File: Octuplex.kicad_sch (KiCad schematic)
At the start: 9 parts, among them U1 MC68B09, U2 MC68B40, U3 MC68B50, U4 27128, U5 HM62256BLP, U6 74LS139, X1 CXO_DIP8, X2 CXO_DIP8

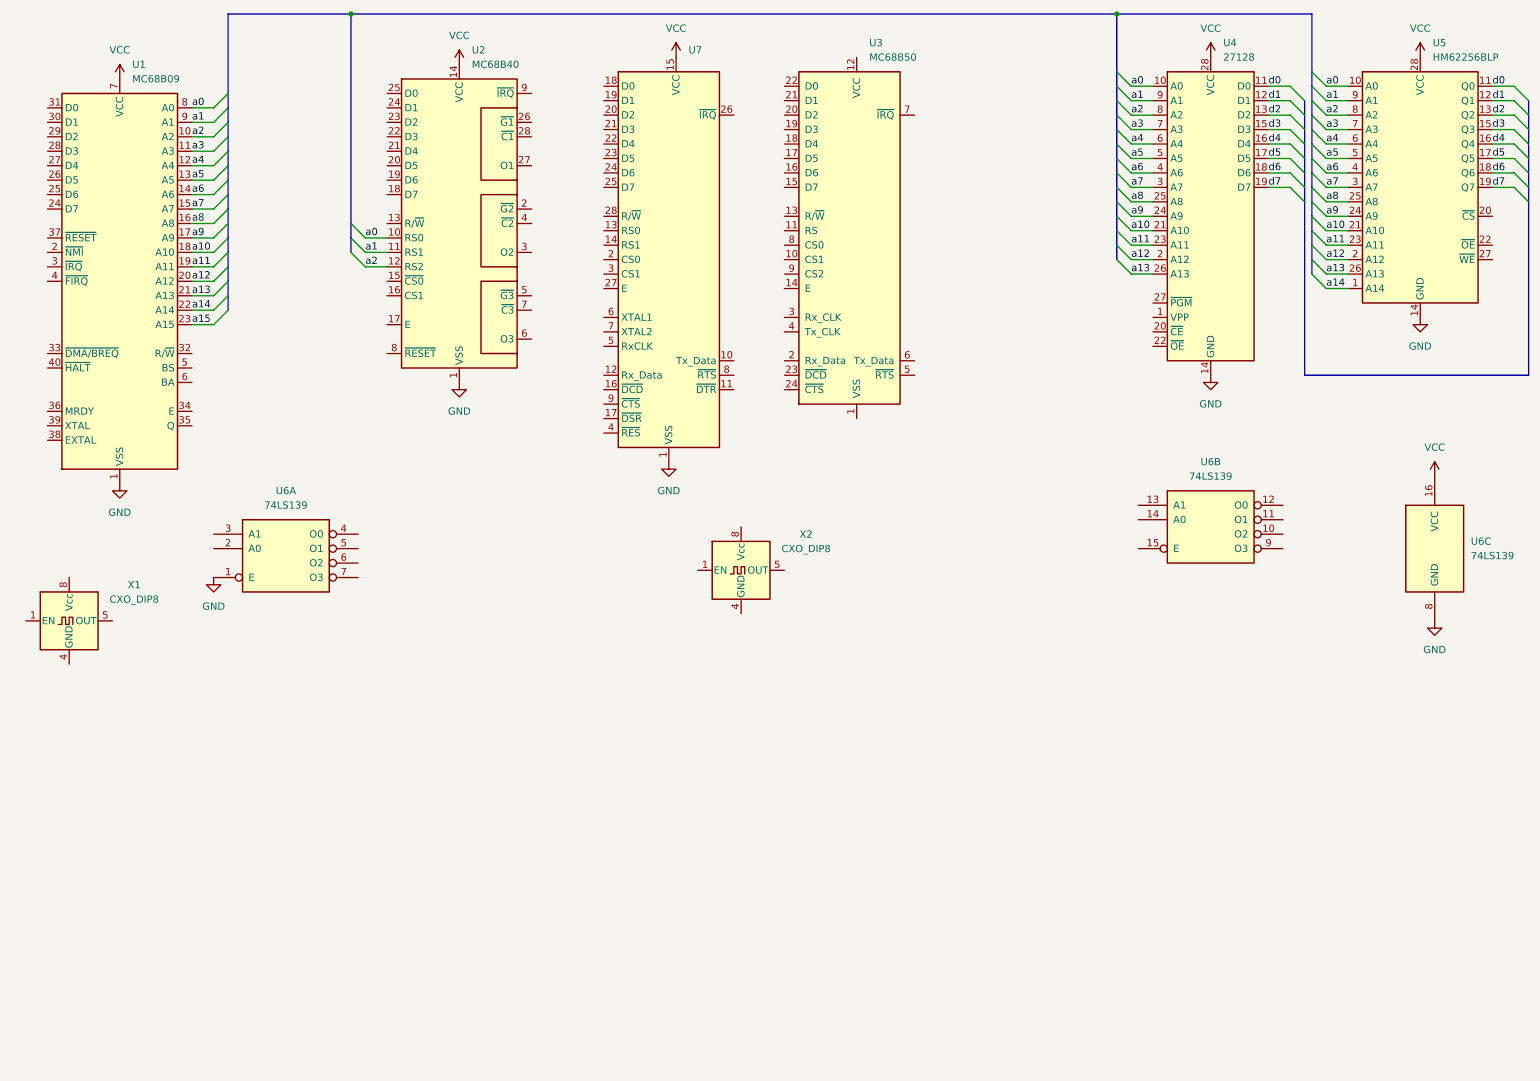
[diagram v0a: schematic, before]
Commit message: WIP: new symbols, initial PCB.
Add 6502 and 6522 symbols. Add mounting holes, board edge, and parts to PCB. Begin wiring up.
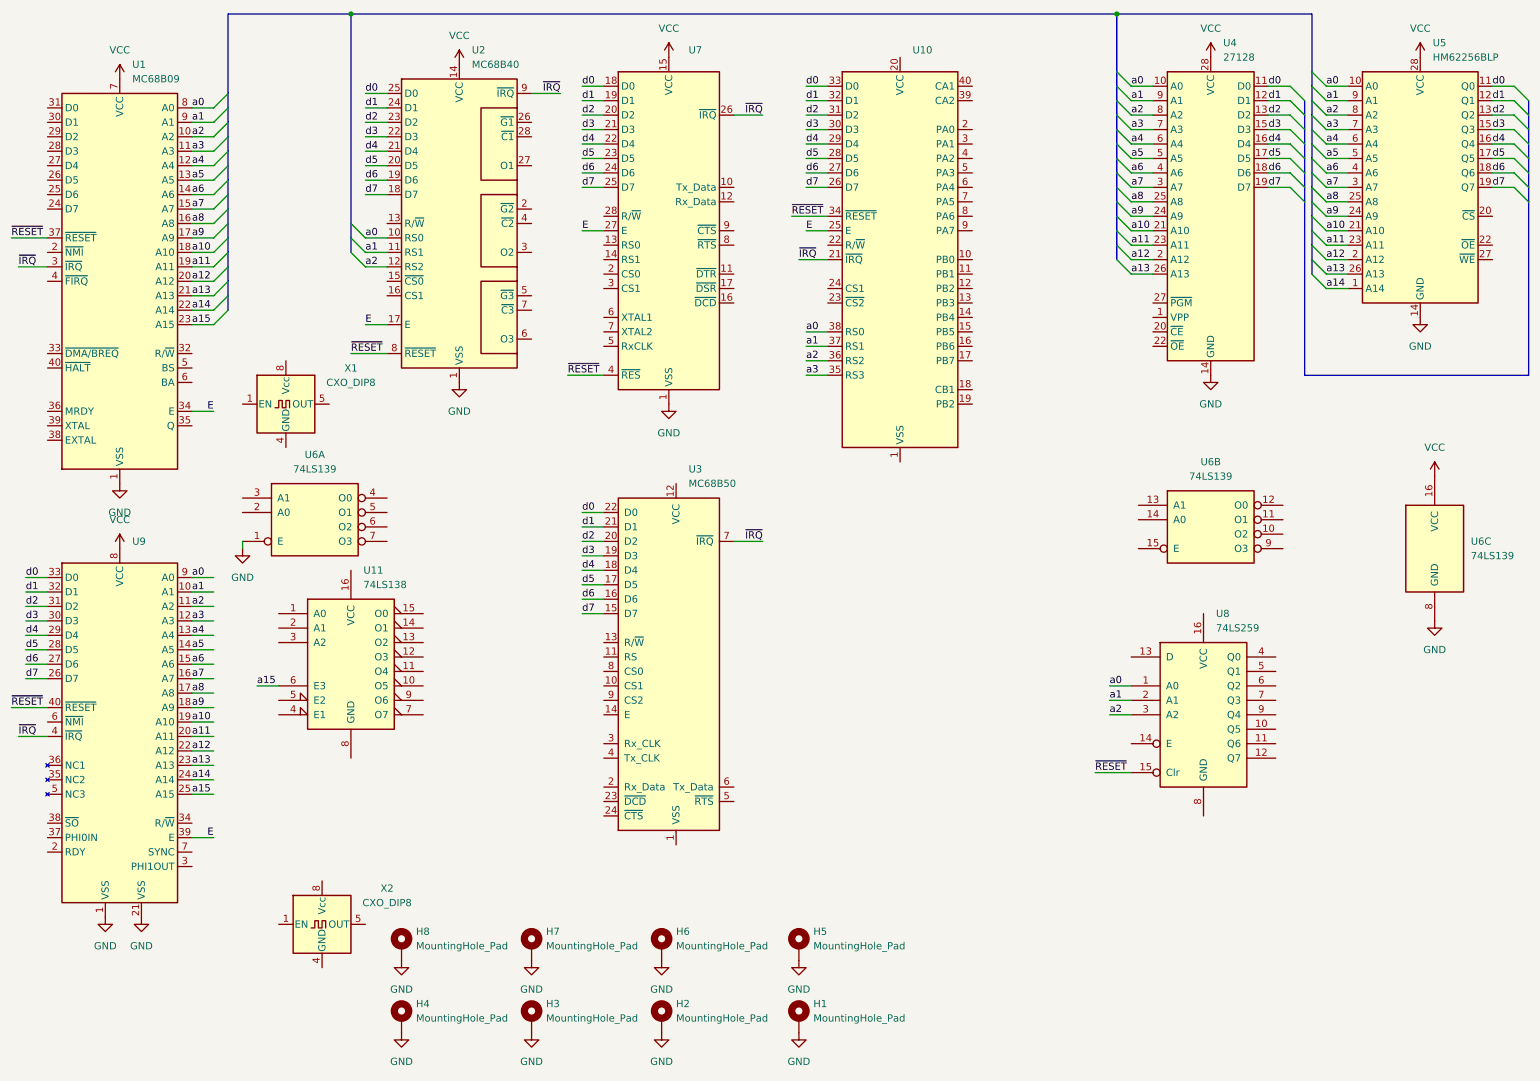
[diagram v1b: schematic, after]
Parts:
- added H1, H2, H3, H4, H5, H6, H7, H8: MountingHole_Pad, MountingHole:MountingHole_3.2mm_M3_Pad, symbol Mechanical:MountingHole_Pad
- added U10: ~, Package_DIP:DIP-40_W15.24mm, symbol Octuplex:R6522
- added U11: 74LS138, Package_DIP:DIP-16_W7.62mm, symbol 74xx:74LS138
- added U8: 74LS259, Package_DIP:DIP-16_W7.62mm, symbol 74xx:74LS259
- added U9: ~, Package_DIP:DIP-40_W15.24mm, symbol Octuplex:M6502
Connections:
- net GND: now also H1.1, H2.1, H3.1, H4.1, H5.1, H6.1, H7.1, H8.1, U9.1 (VSS), U9.21 (VSS)
- net VCC: now also U9.8 (VCC)
- net a0: now also U10.38 (RS0), U8.1 (A0), U9.9 (A0)
- net a1: now also U10.37 (RS1), U8.2 (A1), U9.10 (A1)
- net a10: now also U9.19 (A10)
- net a11: now also U9.20 (A11)
- net a12: now also U9.22 (A12)
- net a13: now also U9.23 (A13)
- net a14: now also U9.24 (A14)
- net a15: now also U11.6 (E3), U9.25 (A15)
- net a2: now also U10.36 (RS2), U8.3 (A2), U9.11 (A2)
- net a3: now also U10.35 (RS3), U9.12 (A3)
- net a4: now also U9.13 (A4)
- net a5: now also U9.14 (A5)
- net a6: now also U9.15 (A6)
- net a7: now also U9.16 (A7)
- net a8: now also U9.17 (A8)
- net a9: now also U9.18 (A9)
- net d0: now also U2.25 (D0), U3.22 (D0), U7.18 (D0), U10.33 (D0), U9.33 (D0)
- net d1: now also U2.24 (D1), U3.21 (D1), U7.19 (D1), U10.32 (D1), U9.32 (D1)
- net d2: now also U2.23 (D2), U3.20 (D2), U7.20 (D2), U10.31 (D2), U9.31 (D2)
- net d3: now also U2.22 (D3), U3.19 (D3), U7.21 (D3), U10.30 (D3), U9.30 (D3)
- net d4: now also U2.21 (D4), U3.18 (D4), U7.22 (D4), U10.29 (D4), U9.29 (D4)
- net d5: now also U2.20 (D5), U3.17 (D5), U7.23 (D5), U10.28 (D5), U9.28 (D5)
- net d6: now also U2.19 (D6), U3.16 (D6), U7.24 (D6), U10.27 (D6), U9.27 (D6)
- net d7: now also U2.18 (D7), U3.15 (D7), U7.25 (D7), U10.26 (D7), U9.26 (D7)
- net ~{IRQ}: now reaches U7.26 (~{IRQ})
- net ~{IRQ}: now also U1.3 (~{IRQ}), U2.9 (~{IRQ}), U3.7 (~{IRQ}), U10.21 (~{IRQ}), U9.4 (~{IRQ})
- net E: now reaches U7.27 (E)
- net E: now also U1.34 (E), U2.17 (E), U10.25 (E), U9.39 (E)
- net ~{RESET}: now reaches U7.4 (~{RES})
- net ~{RESET}: now also U1.37 (~{RESET}), U2.8 (~{RESET}), U10.34 (~{RESET}), U8.15 (Clr), U9.40 (~{RESET})
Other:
- moved on the sheet: U3, U6A, U7, X1, X2

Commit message: Break up schematic into hierarchial sheets.
Connect sheets with address and data buses. TODO: add control bus.
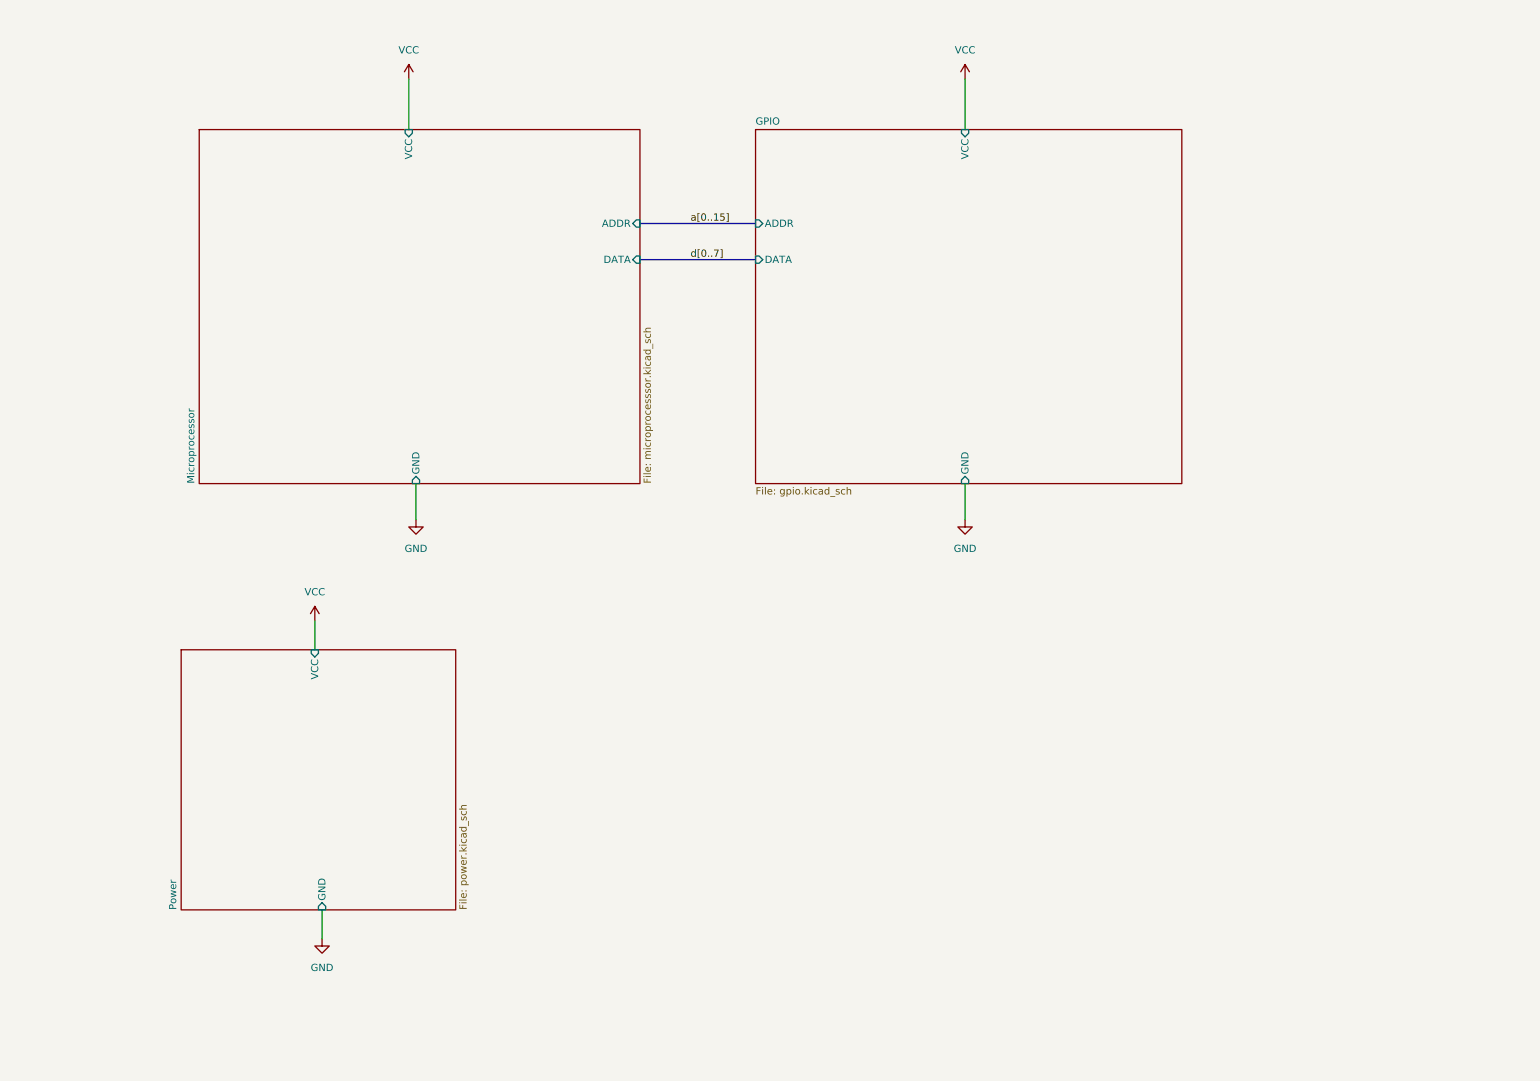
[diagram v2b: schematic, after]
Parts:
- removed H1, H2, H3, H4, H5, H6, H7, H8: MountingHole_Pad, MountingHole:MountingHole_3.2mm_M3_Pad, symbol Mechanical:MountingHole_Pad
- removed U1: MC68B09, Package_DIP:DIP-40_W15.24mm, symbol CPU_NXP_6800:MC68B09
- removed U10: ~, Package_DIP:DIP-40_W15.24mm, symbol Octuplex:R6522
- removed U11: 74LS138, Package_DIP:DIP-16_W7.62mm, symbol 74xx:74LS138
- removed U2: MC68B40, Package_DIP:DIP-28_W15.24mm, symbol Interface:MC68B40
- removed U3: MC68B50, Package_DIP:DIP-24_W15.24mm, symbol Interface_UART:MC68B50
- removed U4: 27128, Package_DIP:DIP-28_W15.24mm, symbol Memory_EPROM:27128
- removed U5: HM62256BLP, Package_DIP:DIP-28_W15.24mm, symbol Memory_RAM:HM62256BLP
- removed U6: 74LS139, Package_DIP:DIP-16_W7.62mm, symbol 74xx:74LS139
- removed U7: ~, Package_DIP:DIP-28_W15.24mm, symbol Octuplex:MXS6551
- removed U8: 74LS259, Package_DIP:DIP-16_W7.62mm, symbol 74xx:74LS259
- removed U9: ~, Package_DIP:DIP-40_W15.24mm, symbol Octuplex:M6502
- removed X1, X2: CXO_DIP8, Oscillator:Oscillator_DIP-8, symbol Oscillator:CXO_DIP8
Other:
- added sheet GPIO (gpio.kicad_sch)
- added sheet Microprocessor (microprocesssor.kicad_sch)
- added sheet Power (power.kicad_sch)
